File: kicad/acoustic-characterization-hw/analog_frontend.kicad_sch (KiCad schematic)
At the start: 27 parts, among them U3 MS9280

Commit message: [kicad] Added connector + input circuit (next) Simulate adc input circuit in ltspice
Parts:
- removed JP7: SolderJumper_2_Bridged, symbol Jumper:SolderJumper_2_Bridged
- added C30, C31: 100 nF +-2%, Capacitor_SMD:C_1206_3216Metric_Pad1.33x1.80mm_HandSolder, symbol Device:C_Small
- added J1: 8P8C_Shielded, Connector_RJ:RJ45_RCH_RC01937, symbol Connector:8P8C_Shielded
- added R16: 50 +-1%, Capacitor_SMD:C_0603_1608Metric_Pad1.08x0.95mm_HandSolder, symbol Device:R_Small
- added R17: 0 +-1%, Resistor_SMD:R_0805_2012Metric_Pad1.20x1.40mm_HandSolder, symbol Device:R_Small
- R15: value 100 -> 50 +- 1 %; LCSC Part Number C22775 -> C23197; Manufacturing Part Number 0603WAF1000T5E -> 0603WAF510JT5E
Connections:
- net ADC_AIN1: now also R17.2; no longer R15.1
- net ADC_REFTS: now also C31.2
- net GNDA: now also J1.SH
- net ADC_VDDA_2: now reaches R13.2, R14.1
- net ADC_VDDA_2: now also R15.1, R16.2
- new net: C30.2, R16.1, R17.1
- new net: C31.1, J1.4
- new net: C30.1, J1.5
- no-connect marks 0 -> 6
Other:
- note added: "- Differential impedance: 100 ohms - Input capacitance: 300 nF, f_plateau = 1/[2*pi*C*(R_diff/2)] = 30 kHz Max offst: 4% <<<< 1´ @ 1 MHz - Added 0-ohm series resistor in case of single-ended operation (LC damping)"
- moved on the sheet: C16, C17, C22, C23, C24, C25, JP1, JP11, JP2, JP3, R11, R12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

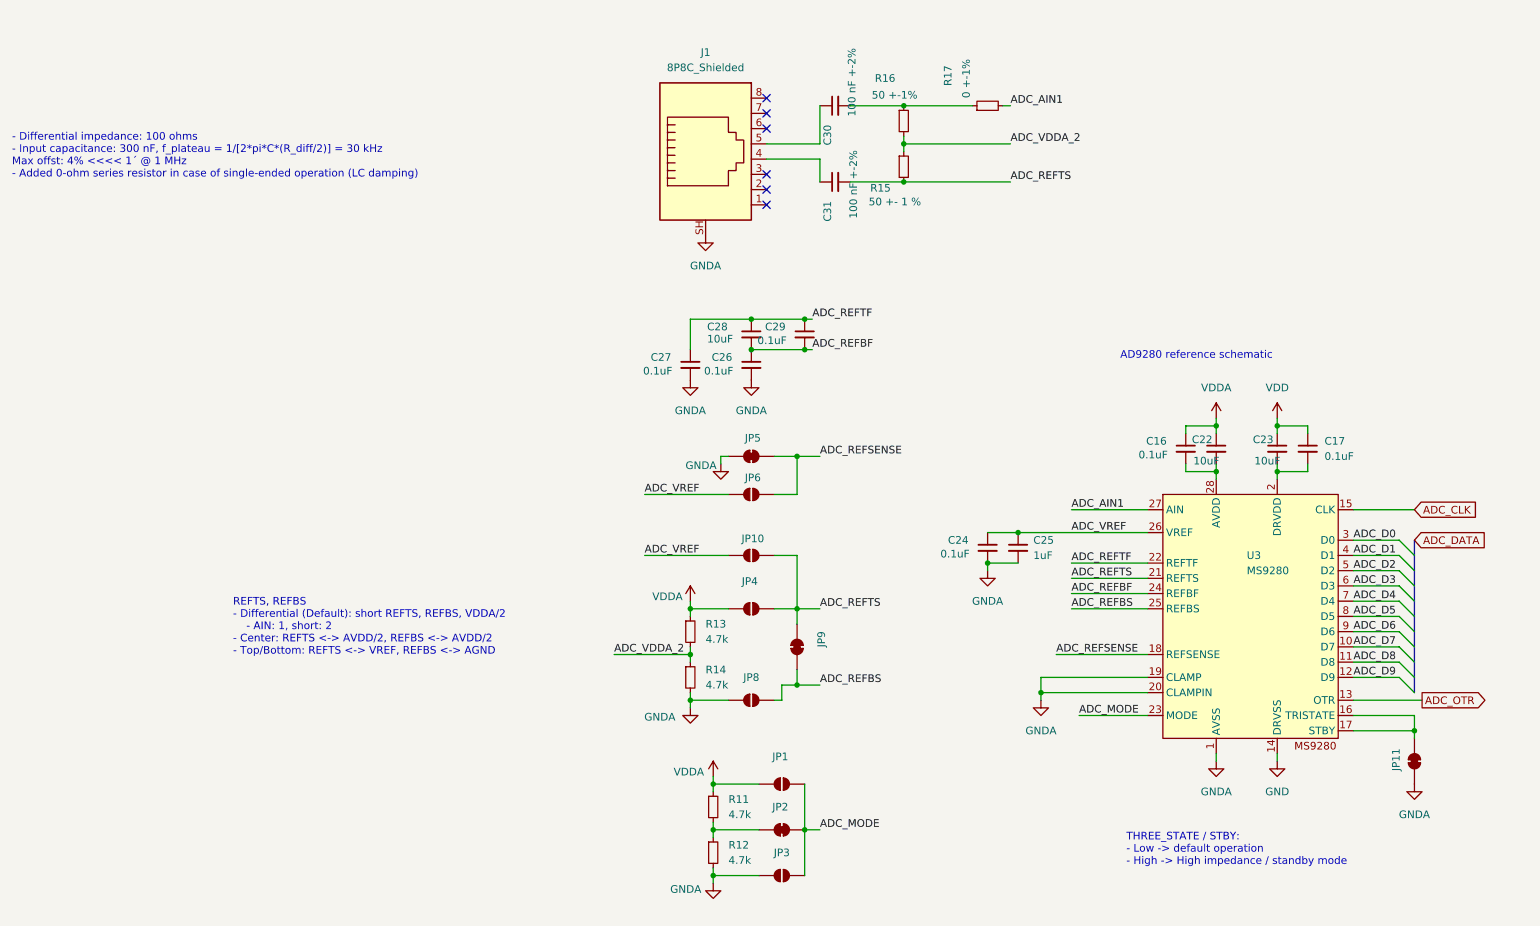
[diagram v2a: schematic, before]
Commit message: [kicad] Connected DDR3L bus, added info on FPGA and ddr pin functionality (next) add filtering circuitry for DDR power pins
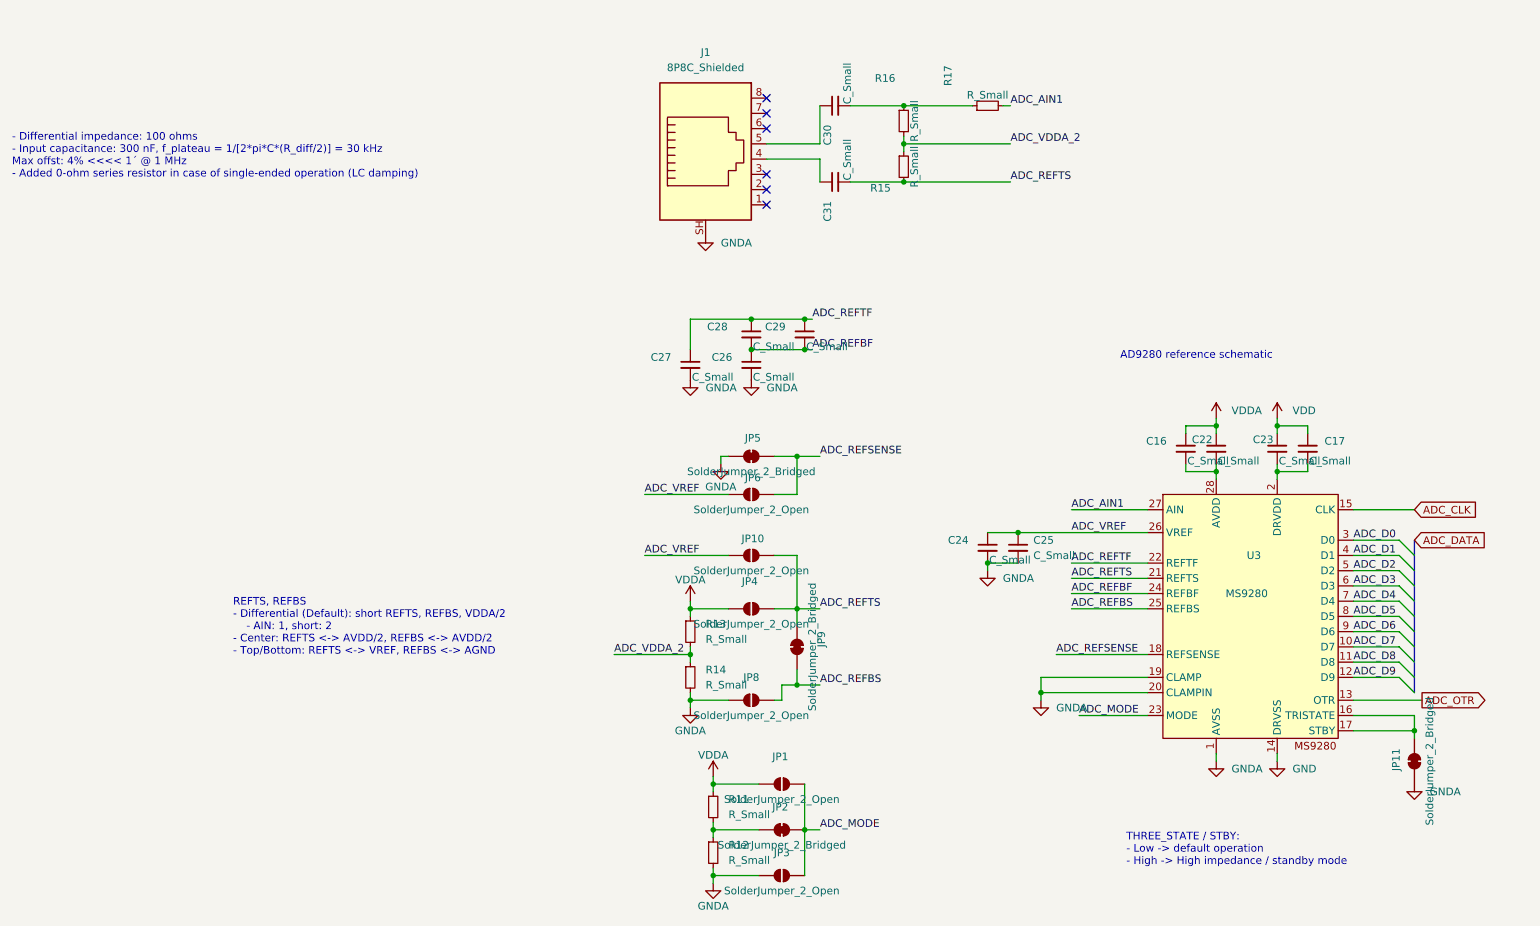
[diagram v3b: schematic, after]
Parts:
- C16, C17, C24, C26, C27, C29: value 0.1uF -> C_Small
- C22, C23, C28: value 10uF -> C_Small
- C25: value 1uF -> C_Small
- C30, C31: value 100 nF +-2% -> C_Small
- R11, R12, R13, R14: value 4.7k -> R_Small
- R15: value 50 +- 1 % -> R_Small
- R16: value 50 +-1% -> R_Small
- R17: value 0 +-1% -> R_Small

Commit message: [kicad] re-added passive values after accidental removal
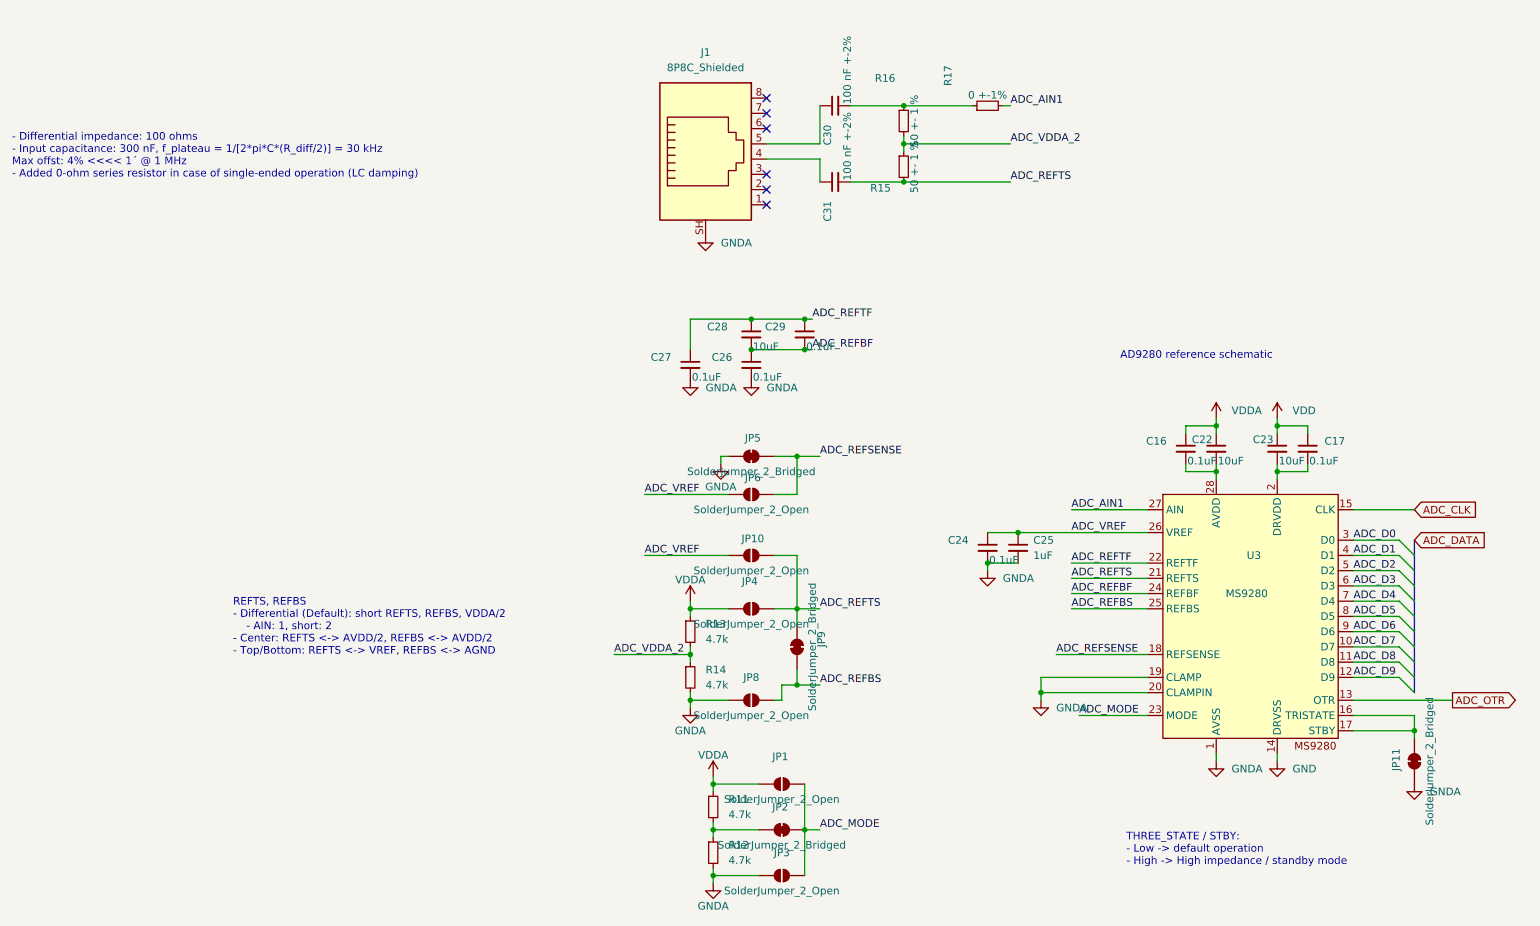
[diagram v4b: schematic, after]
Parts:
- C16, C17, C24, C26, C27, C29: value C_Small -> 0.1uF
- C22, C23, C28: value C_Small -> 10uF
- C25: value C_Small -> 1uF
- C30, C31: value C_Small -> 100 nF +-2%
- R11, R12, R13, R14: value R_Small -> 4.7k
- R15, R16: value R_Small -> 50 +- 1 %
- R17: value R_Small -> 0 +-1%
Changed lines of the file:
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@@
 	(wire
 		(pts
-			(xy 135.89 160.02) (xy 147.32 160.02)
+			(xy 135.89 160.02) (xy 152.4 160.02)
 		)
 		(stroke
@@
 	(global_label "ADC_OTR"
 		(shape output)
-		(at 147.32 160.02 0)
+		(at 152.4 160.02 0)
 		(fields_autoplaced yes)
 		(effects
@@
 		)
 		(property "Intersheetrefs" "${INTERSHEET_REFS}"
-			(at 158.4695 160.02 0)
+			(at 163.5495 160.02 0)
 			(effects
 				(font
@@
 			)
 		)
-		(property "Value" "C_Small"
+		(property "Value" "0.1uF"
 			(at 75.184 136.652 0)
 			(effects
@@
 			)
 		)
-		(property "Value" "C_Small"
+		(property "Value" "10uF"
 			(at 113.284 120.142 0)
 			(effects
@@
 			)
 		)
-		(property "Value" "R_Small"
+		(property "Value" "0 +-1%"
 			(at 74.93 59.182 90)
 			(effects
@@
 			)
 		)
-		(property "Value" "C_Small"
+		(property "Value" "10uF"
 			(at 35.814 101.092 0)
 			(effects
@@
 			)
 		)
-		(property "Value" "C_Small"
+		(property "Value" "0.1uF"
 			(at 25.654 106.172 0)
 			(effects
@@
 			)
 		)
-		(property "Value" "C_Small"
+		(property "Value" "0.1uF"
 			(at 108.204 120.142 0)
 			(effects
@@
 			)
 		)
-		(property "Value" "C_Small"
+		(property "Value" "1uF"
 			(at 82.55 135.8962 0)
 			(effects
@@
 			)
 		)
-		(property "Value" "C_Small"
+		(property "Value" "100 nF +-2%"
 			(at 51.562 73.406 0)
 			(effects
@@
 			)
 		)
-		(property "Value" "C_Small"
+		(property "Value" "10uF"
 			(at 123.444 120.142 0)
 			(effects
@@
 			)
 		)
-		(property "Value" "R_Small"
+		(property "Value" "50 +- 1 %"
 			(at 62.738 63.5 90)
 			(effects
@@
 			)
 		)
-		(property "Value" "C_Small"
+		(property "Value" "0.1uF"
 			(at 35.814 106.172 0)
 			(effects
@@
 			)
 		)
-		(property "Value" "R_Small"
+		(property "Value" "4.7k"
 			(at 31.75 179.0699 0)
 			(effects
@@
 			)
 		)
-		(property "Value" "R_Small"
+		(property "Value" "4.7k"
 			(at 27.94 149.8599 0)
 			(effects
@@
 			)
 		)
-		(property "Value" "R_Small"
+		(property "Value" "50 +- 1 %"
 			(at 62.738 71.12 90)
 			(effects
@@
 			)
 		)
-		(property "Value" "R_Small"
+		(property "Value" "4.7k"
 			(at 27.94 157.4799 0)
 			(effects
@@
 			)
 		)
-		(property "Value" "R_Small"
+		(property "Value" "4.7k"
 			(at 31.75 186.6899 0)
 			(effects
@@
 			)
 		)
-		(property "Value" "C_Small"
+		(property "Value" "0.1uF"
 			(at 44.704 101.092 0)
 			(effects
@@
 			)
 		)
-		(property "Value" "C_Small"
+		(property "Value" "100 nF +-2%"
 			(at 51.562 60.706 0)
 			(effects
@@
 			)
 		)
-		(property "Value" "C_Small"
+		(property "Value" "0.1uF"
 			(at 128.524 120.142 0)
 			(effects
